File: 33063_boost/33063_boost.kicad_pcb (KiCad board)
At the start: 2 copper layers, 47 x 20 mm, 15 parts, among them J1 Conn_01x02, J2 Conn_01x02, U1 33063

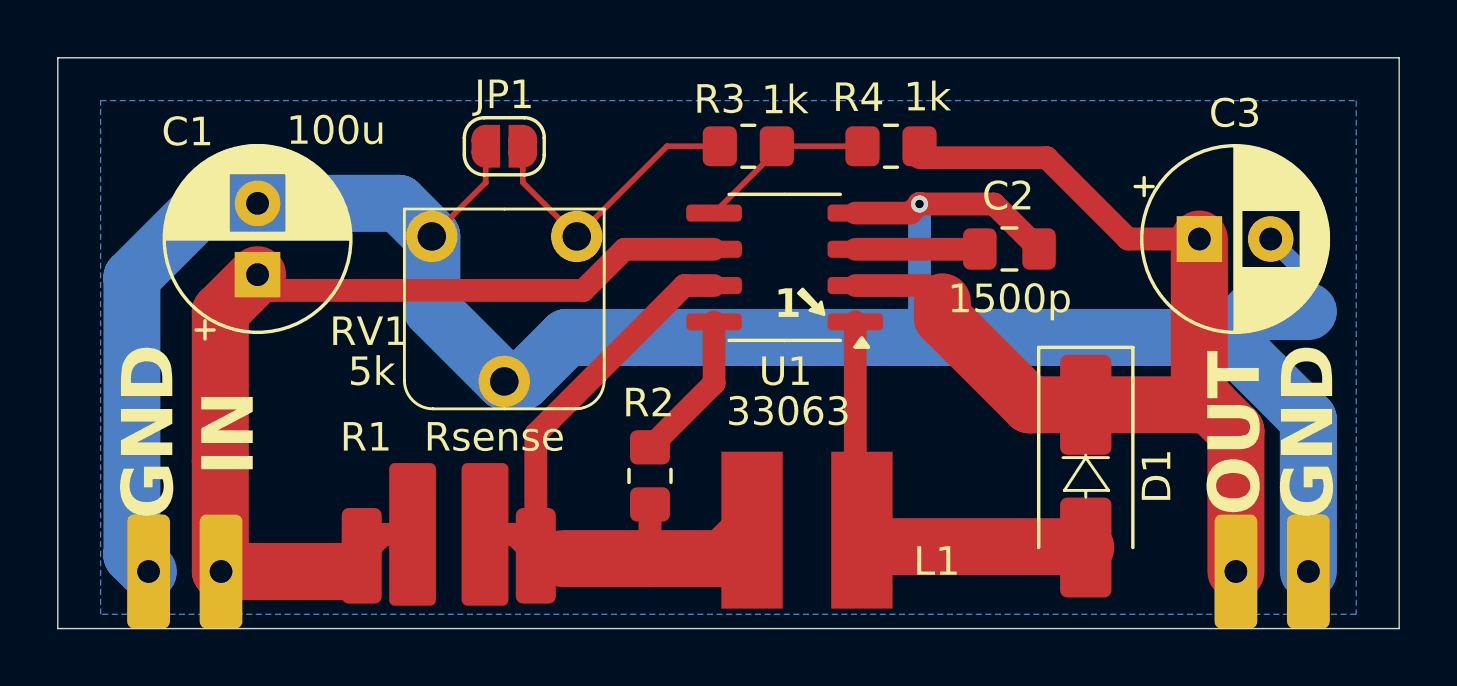
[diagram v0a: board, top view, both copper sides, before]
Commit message: added DFN breakout changed trim pot type in 33063_boost, 33063_invert, r1283_power boards fixed error in 33063_boost board (move trim pot to higher side of voltage divider)
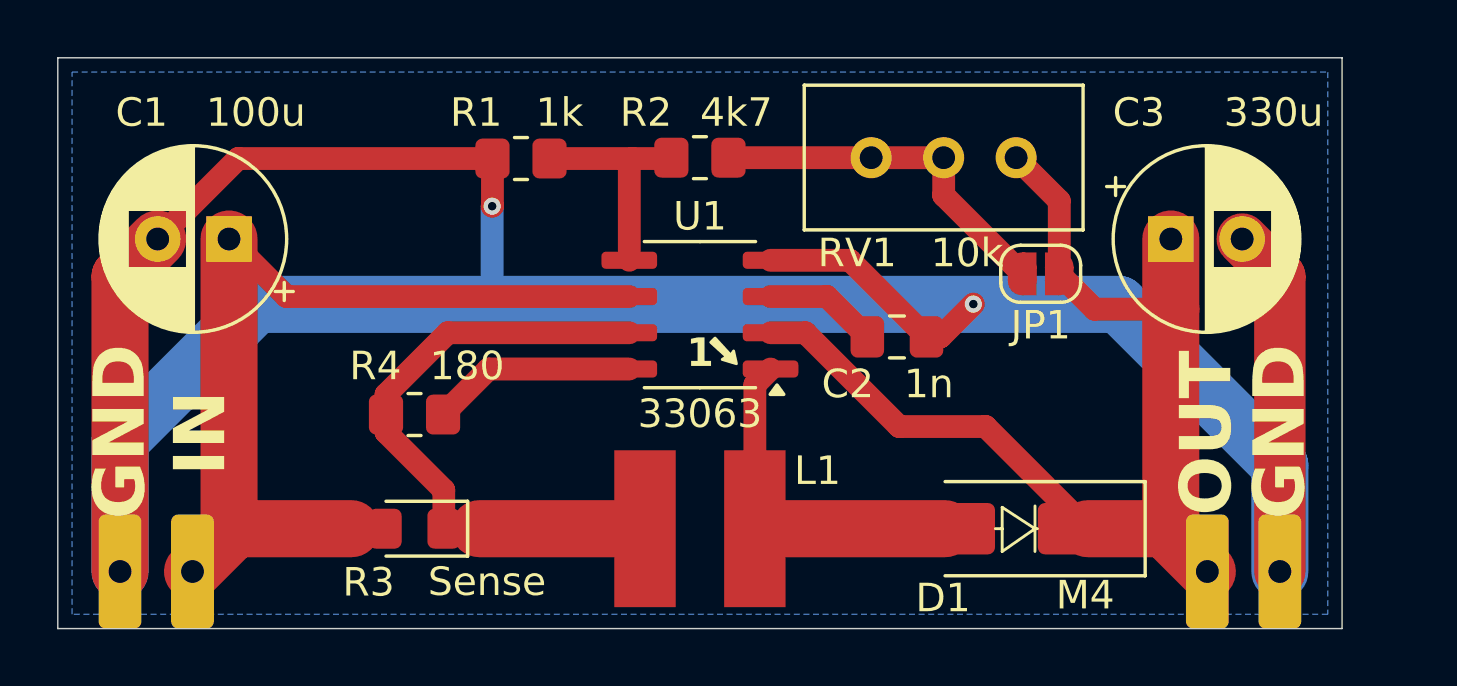
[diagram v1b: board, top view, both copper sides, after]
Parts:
- removed R100: 1, misc:0805_5mm
- C2: value 1500p -> 1n
- L1: value L -> 220uH
- R2: renamed from R4; value 1k -> 4k7
- R3: renamed from R1; value Rsense -> Sense; footprint Resistor_SMD:R_2512_6332Metric_Pad1.40x3.35mm_HandSolder -> LED_SMD:LED_0805_2012Metric_Pad1.15x1.40mm_HandSolder
- RV1: value 5k -> 10k; footprint misc:trim_pot -> Potentiometer_THT:Potentiometer_Bourns_3296W_Vertical
- moved JP1 19.3 mm to (84.4, 57.6), turned to 180 degrees
- moved RV1 13.9 mm to (78.5, 53.5)
- moved R4 8.53 mm to (62.5, 62.5), turned to 0 degrees
- moved R1 7.98 mm to (66.2, 53.5)
- moved R2 6.71 mm to (72.5, 53.5)
- moved C2 5.00 mm to (79.4, 59.8)
- moved L1 3.75 mm to (72.5, 66.5)
- moved U1 3.40 mm to (72.5, 59.0)
- moved D1 3.05 mm to (83.6, 66.5), turned to 180 degrees
- moved C1 1.60 mm to (56.0, 56.4), turned to 180 degrees
- moved R3 1.53 mm to (62.5, 66.5)
- moved C3 1.00 mm to (89.0, 56.4)
- moved J1 1.00 mm to (53.5, 70.0)
- moved J2 1.00 mm to (91.5, 70.0)
- renumbered R3 to R1, R2 to R4
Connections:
- JP1 pad 1: GND1 -> /Vout
- R1 pad 1: Net-(JP1-B) -> GND1
- R2 pad 2: /Vout -> Net-(JP1-B)
- RV1 pad 2: GND1 -> Net-(JP1-B)
- RV1 pad 3: GND1 -> /Vout
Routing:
- net GND1: track 90.0 -> 104.4 mm, vias 1 -> 2
- net /Lout: track 15.5 -> 12.5 mm
- net /Lin: track 24.7 -> 22.0 mm
- net /Vin: track 35.0 -> 32.5 mm
- net Net-(JP1-B): track 10.3 -> 12.7 mm
- net Net-(U1-Dc): track 5.40 -> 7.19 mm
- net /Vfb: track 6.25 -> 7.89 mm
- net /Vout: track 37.6 -> 38.1 mm
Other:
- board size 47 x 20 mm -> 45 x 20 mm
- board text added: "L1"
- board text added: "Vout = 1.25 * (1 + (R2 + RV1) / R1)"
- board text removed: "Vout = 1.25 * (1 + R4 / R3)"
